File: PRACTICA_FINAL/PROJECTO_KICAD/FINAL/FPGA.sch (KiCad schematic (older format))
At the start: 0 parts

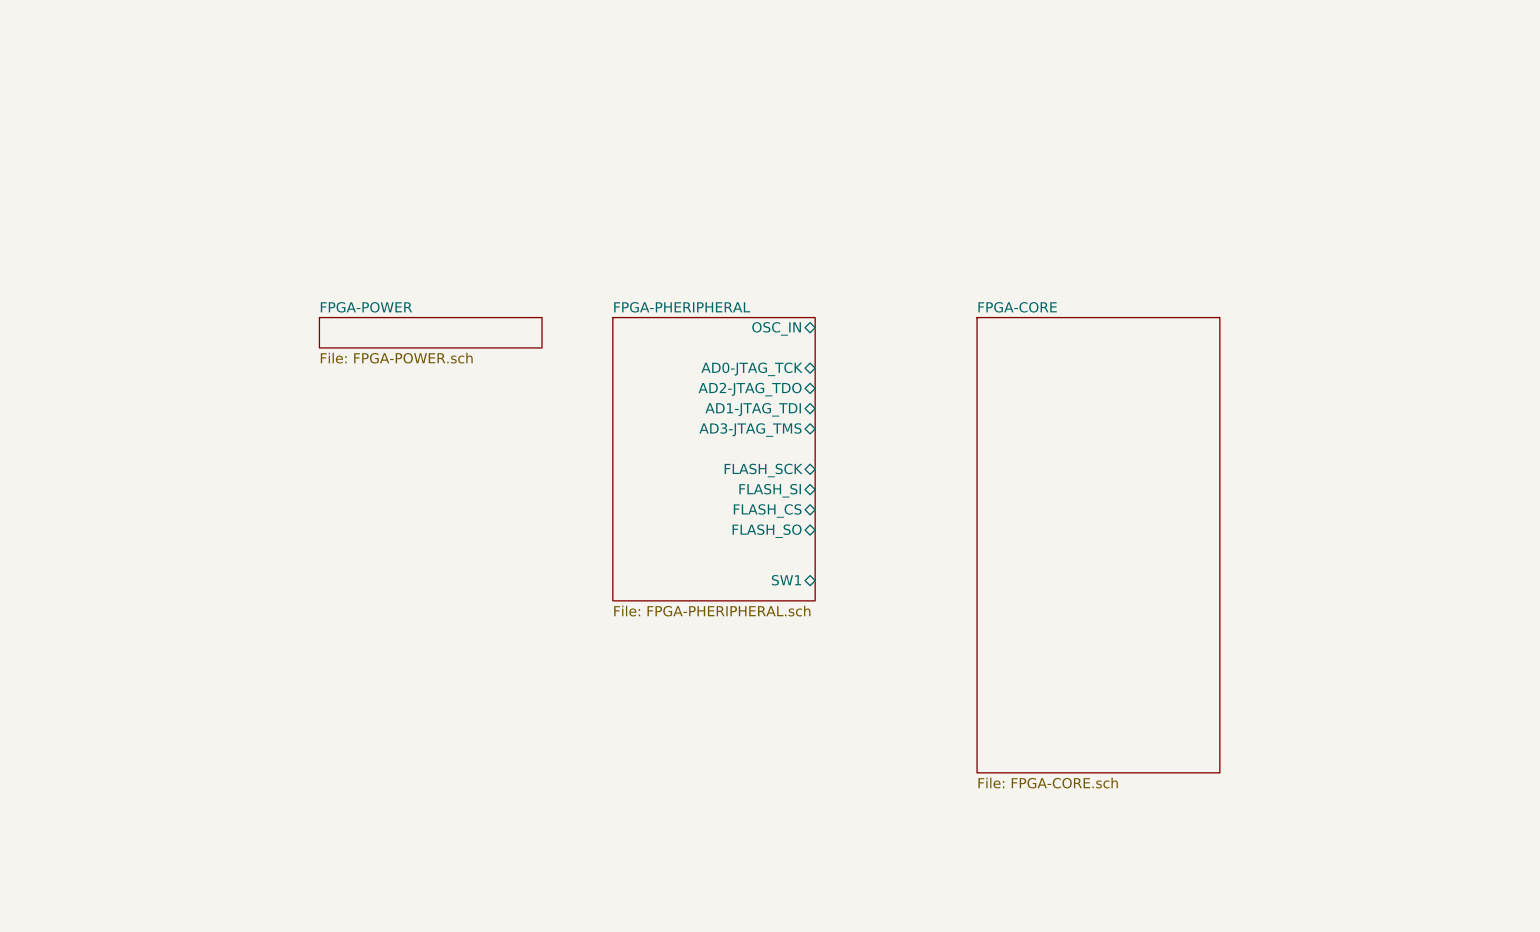
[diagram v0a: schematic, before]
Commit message: Actualizado el esquematico se enumera igual que el pdf. Se asignan todas las huellas lo unico que falta es la huella de un Arduino superpuesto Se corre DRC de esquematico y tambien se pasa a .NET y se levanta en el Kicad PCB sin errores
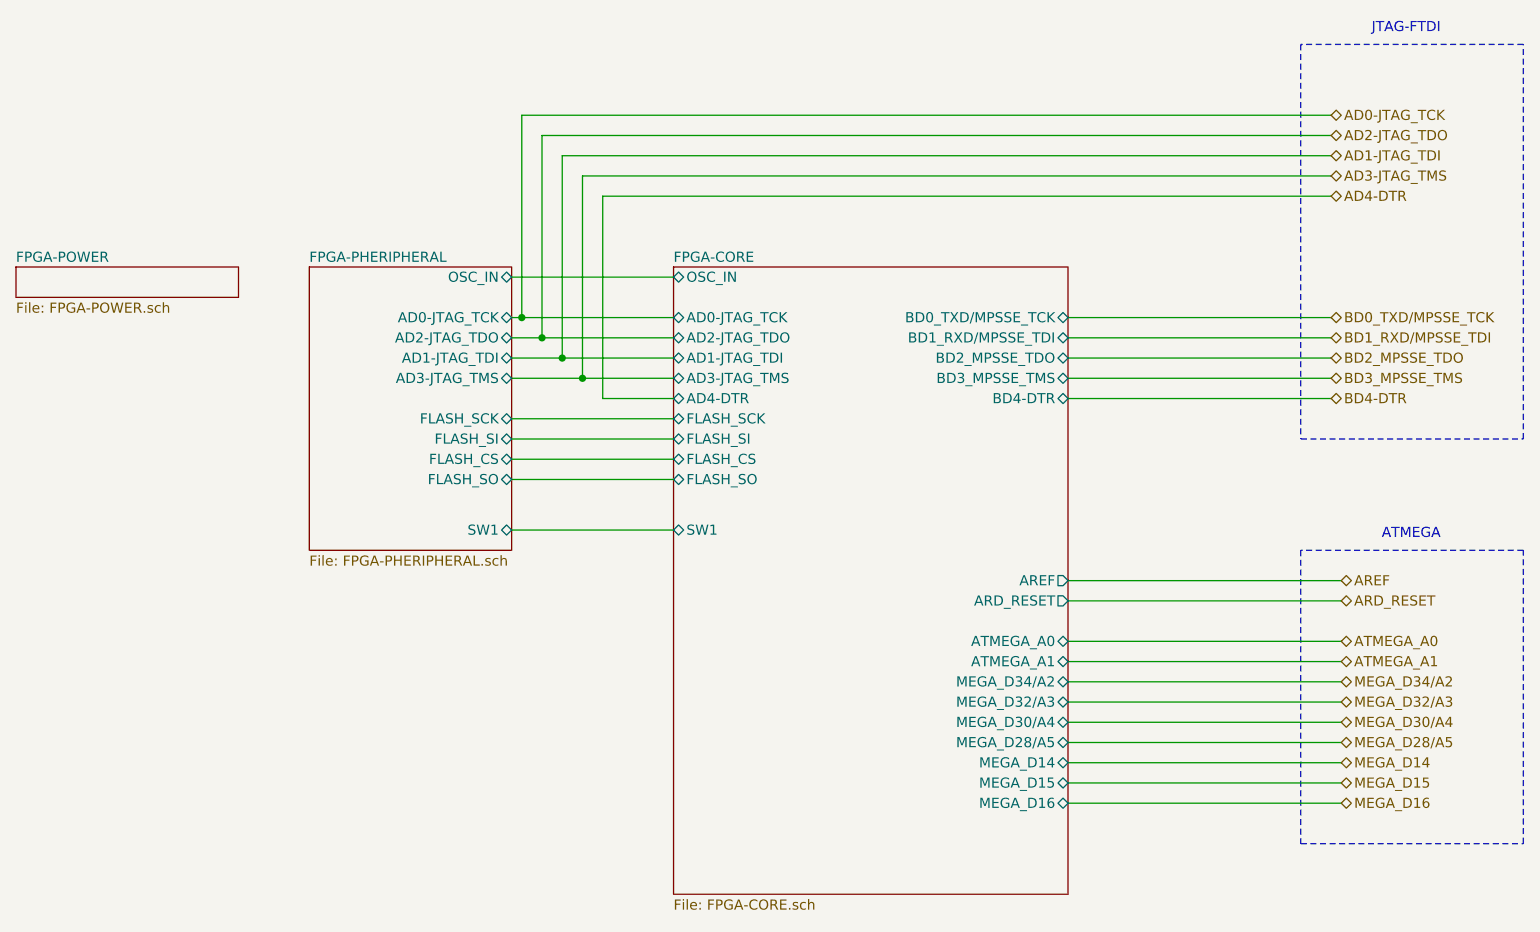
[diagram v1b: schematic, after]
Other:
- note added: "ATMEGA"
- note added: "JTAG-FTDI"
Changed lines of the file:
@@
 $EndDescr
 $Sheet
-S 3650 3000 1100 150
+S 2150 2750 1100 150
 U 5BBCECAD
 F0 "FPGA-POWER" 50
@@
 $EndSheet
 $Sheet
-S 5100 3000 1000 1400
+S 3600 2750 1000 1400
 U 5BBCECB0
 F0 "FPGA-PHERIPHERAL" 50
 F1 "FPGA-PHERIPHERAL.sch" 50
-F2 "OSC_IN" B R 6100 3050 50
-F3 "AD0-JTAG_TCK" B R 6100 3250 50
-F4 "AD2-JTAG_TDO" B R 6100 3350 50
-F5 "AD1-JTAG_TDI" B R 6100 3450 50
-F6 "AD3-JTAG_TMS" B R 6100 3550 50
-F7 "FLASH_SCK" B R 6100 3750 50
-F8 "FLASH_SI" B R 6100 3850 50
-F9 "FLASH_CS" B R 6100 3950 50
-F10 "FLASH_SO" B R 6100 4050 50
-F11 "SW1" B R 6100 4300 50
+F2 "OSC_IN" B R 4600 2800 50
+F3 "AD0-JTAG_TCK" B R 4600 3000 50
+F4 "AD2-JTAG_TDO" B R 4600 3100 50
+F5 "AD1-JTAG_TDI" B R 4600 3200 50
+F6 "AD3-JTAG_TMS" B R 4600 3300 50
+F7 "FLASH_SCK" B R 4600 3500 50
+F8 "FLASH_SI" B R 4600 3600 50
+F9 "FLASH_CS" B R 4600 3700 50
+F10 "FLASH_SO" B R 4600 3800 50
+F11 "SW1" B R 4600 4050 50
 $EndSheet
 $Sheet
-S 6900 3000 1200 2250
+S 5400 2750 1950 3100
 U 5BBCECB3
 F0 "FPGA-CORE" 50
 F1 "FPGA-CORE.sch" 50
+F2 "ARD_RESET" O R 7350 4400 50
+F3 "ATMEGA_A0" B R 7350 4600 50
+F4 "ATMEGA_A1" B R 7350 4700 50
+F5 "MEGA_D34/A2" B R 7350 4800 50
+F6 "MEGA_D32/A3" B R 7350 4900 50
+F7 "MEGA_D30/A4" B R 7350 5000 50
+F8 "MEGA_D28/A5" B R 7350 5100 50
+F9 "AD0-JTAG_TCK" B L 5400 3000 50
+F10 "AD1-JTAG_TDI" B L 5400 3200 50
+F11 "AD2-JTAG_TDO" B L 5400 3100 50
+F12 "AD3-JTAG_TMS" B L 5400 3300 50
+F13 "AD4-DTR" B L 5400 3400 50
+F14 "BD0_TXD/MPSSE_TCK" B R 7350 3000 50
+F15 "FLASH_CS" B L 5400 3700 50
+F16 "FLASH_SCK" B L 5400 3500 50
+F17 "FLASH_SI" B L 5400 3600 50
+F18 "FLASH_SO" B L 5400 3800 50
+F19 "SW1" B L 5400 4050 50
+F20 "OSC_IN" B L 5400 2800 50
+F21 "MEGA_D14" B R 7350 5200 50
+F22 "MEGA_D15" B R 7350 5300 50
+F23 "MEGA_D16" B R 7350 5400 50
+F24 "BD3_MPSSE_TMS" B R 7350 3300 50
+F25 "BD4-DTR" B R 7350 3400 50
+F26 "BD2_MPSSE_TDO" B R 7350 3200 50
+F27 "BD1_RXD/MPSSE_TDI" B R 7350 3100 50
+F28 "AREF" O R 7350 4300 50
 $EndSheet
+Wire Wire Line
+	4600 2800 5400 2800
+Wire Wire Line
+	4600 3000 4650 3000
+Wire Wire Line
+	4600 3100 4750 3100
+Wire Wire Line
+	4600 3200 4850 3200
+Wire Wire Line
+	4600 3300 4950 3300
+Wire Wire Line
+	4600 3500 5400 3500
+Wire Wire Line
+	4600 3600 5400 3600
+Wire Wire Line
+	4600 3700 5400 3700
+Wire Wire Line
+	4600 3800 5400 3800
+Wire Wire Line
+	4600 4050 5400 4050
+Wire Wire Line
+	7350 3000 8650 3000
+Wire Wire Line
+	7350 3100 8650 3100
+Wire Wire Line
+	7350 3200 8650 3200
+Wire Wire Line
+	7350 3300 8650 3300
+Wire Wire Line
+	7350 3400 8650 3400
+Wire Wire Line
+	5400 3400 5050 3400
+Wire Wire Line
+	5050 3400 5050 2400
+Wire Wire Line
+	5050 2400 8650 2400
+Wire Wire Line
+	4950 3300 4950 2300
+Wire Wire Line
+	4950 2300 8650 2300
+Connection ~ 4950 3300
+Wire Wire Line
+	4950 3300 5400 3300
+Wire Wire Line
+	4850 3200 4850 2200
+Wire Wire Line
+	4850 2200 8650 2200
+Connection ~ 4850 3200
+Wire Wire Line
+	4850 3200 5400 3200
+Wire Wire Line
+	4750 3100 4750 2100
+Wire Wire Line
+	4750 2100 8650 2100
+Connection ~ 4750 3100
+Wire Wire Line
+	4750 3100 5400 3100
+Wire Wire Line
+	4650 3000 4650 2000
+Wire Wire Line
+	4650 2000 8650 2000
+Connection ~ 4650 3000
+Wire Wire Line
+	4650 3000 5400 3000
+Text HLabel 8650 2000 2    50   BiDi ~ 0
+AD0-JTAG_TCK
+Text HLabel 8650 2100 2    50   BiDi ~ 0
+AD2-JTAG_TDO
+Text HLabel 8650 2200 2    50   BiDi ~ 0
+AD1-JTAG_TDI
+Text HLabel 8650 2300 2    50   BiDi ~ 0
+AD3-JTAG_TMS
+Text HLabel 8650 2400 2    50   BiDi ~ 0
+AD4-DTR
+Text HLabel 8650 3000 2    50   BiDi ~ 0
+BD0_TXD/MPSSE_TCK
+Text HLabel 8650 3100 2    50   BiDi ~ 0
+BD1_RXD/MPSSE_TDI
+Text HLabel 8650 3200 2    50   BiDi ~ 0
+BD2_MPSSE_TDO
+Text HLabel 8650 3300 2    50   BiDi ~ 0
+BD3_MPSSE_TMS
+Text HLabel 8650 3400 2    50   BiDi ~ 0
+BD4-DTR
+Wire Notes Line
+	8500 1650 8500 3600
+Wire Notes Line
+	8500 3600 9600 3600
+Wire Notes Line
+	9600 3600 9600 1650
+Wire Notes Line
+	9600 1650 8500 1650
+Text Notes 8850 1600 0    50   ~ 0
+JTAG-FTDI
+Wire Wire Line
+	7350 4300 8700 4300
+Wire Wire Line
+	7350 4400 8700 4400
+Wire Wire Line
+	7350 4600 8700 4600
+Wire Wire Line
+	7350 4700 8700 4700
+Wire Wire Line
+	7350 4800 8700 4800
+Wire Wire Line
+	7350 4900 8700 4900
+Wire Wire Line
+	7350 5000 8700 5000
+Wire Wire Line
+	7350 5100 8700 5100
+Wire Wire Line
+	7350 5200 8700 5200
+Wire Wire Line
+	7350 5300 8700 5300
+Wire Wire Line
+	7350 5400 8700 5400
+Text HLabel 8700 4300 2    50   BiDi ~ 0
+AREF
+Text HLabel 8700 4400 2    50   BiDi ~ 0
+ARD_RESET
+Text HLabel 8700 4600 2    50   BiDi ~ 0
+ATMEGA_A0
+Text HLabel 8700 4700 2    50   BiDi ~ 0
+ATMEGA_A1
+Text HLabel 8700 4800 2    50   BiDi ~ 0
+MEGA_D34/A2
+Text HLabel 8700 4900 2    50   BiDi ~ 0
+MEGA_D32/A3
+Text HLabel 8700 5000 2    50   BiDi ~ 0
+MEGA_D30/A4
+Text HLabel 8700 5100 2    50   BiDi ~ 0
+MEGA_D28/A5
+Text HLabel 8700 5200 2    50   BiDi ~ 0
+MEGA_D14
+Text HLabel 8700 5300 2    50   BiDi ~ 0
+MEGA_D15
+Text HLabel 8700 5400 2    50   BiDi ~ 0
+MEGA_D16
+Wire Notes Line
+	8500 4150 8500 5600
+Wire Notes Line
+	8500 5600 9600 5600
+Wire Notes Line
+	9600 5600 9600 4150
+Wire Notes Line
+	9600 4150 8500 4150
+Text Notes 8900 4100 0    50   ~ 0
+ATMEGA
 $EndSCHEMATC
